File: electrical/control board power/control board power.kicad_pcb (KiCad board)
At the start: 2 copper layers, 147.3 x 147.3 mm, 67 parts, among them J1 Conn_01x02, J10 48V_from_conversion, J11 Aux_2, J17 Switch_B, J2 5V, J3 Barrel_Jack, J4 Switch_A, J5 Switch_Input, J6 Power_Connector, J7 Switch_A_High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

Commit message: stuff
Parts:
- moved Q2 6.48 mm to (132.0, 63.1)
- moved J17 5.21 mm to (141.4, 82.4)
- moved C24 5.08 mm to (139.6, 91.9)
- moved J8 5.08 mm to (134.5, 87.6)
- moved D10 3.86 mm to (133.0, 79.5)
- moved J4 2.03 mm to (124.2, 82.4)
- moved D9 1.17 mm to (116.1, 79.6)
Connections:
- C23 pad 1: Net-(C23-Pad1) -> GND
- C24 pad 1: Net-(C23-Pad1) -> GND
- Q1 pad 3: Net-(C23-Pad1) -> GND
- Q2 pad 3: Net-(C23-Pad1) -> GND
- R4 pad 2: Net-(C23-Pad1) -> GND
- R5 pad 2: Net-(C23-Pad1) -> GND
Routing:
- net GND: track 111.8 -> 122.8 mm, vias 69 -> 75
- net +24V: track 227.7 -> 218.9 mm
- net Net-(C23-Pad1): track 8.21 -> 0.00 mm, vias 6 -> 0
- net /SWITCH_B: track 16.4 -> 23.4 mm
- net +5V: track 289.4 -> 284.4 mm
- net Net-(C7-Pad1): track 14.7 -> 11.6 mm
- net Net-(C8-Pad2): track 12.4 -> 9.75 mm
- net /SWITCH_B_HIGH: track 18.3 -> 21.0 mm
- net /SWITCH_A_HIGH: track 19.6 -> 21.4 mm
- net Net-(D9-Pad2): track 18.8 -> 19.3 mm

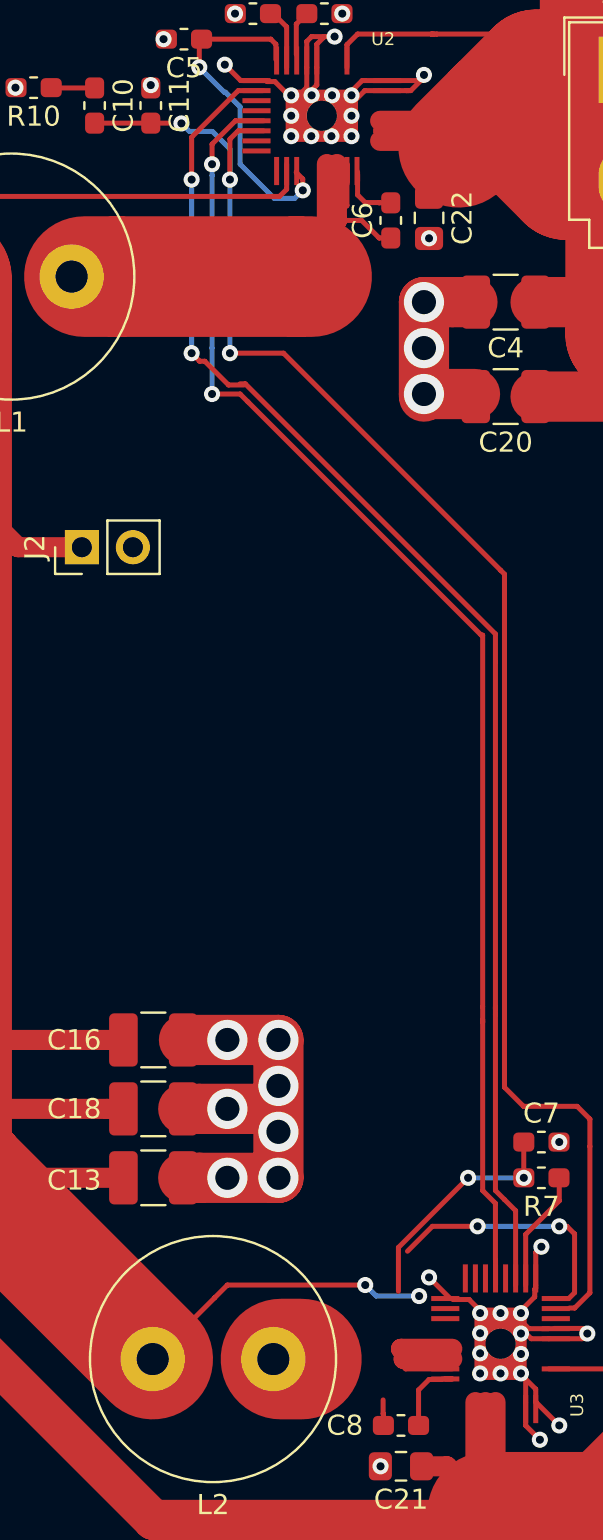
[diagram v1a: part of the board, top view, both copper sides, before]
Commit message: fixed unconnected parts
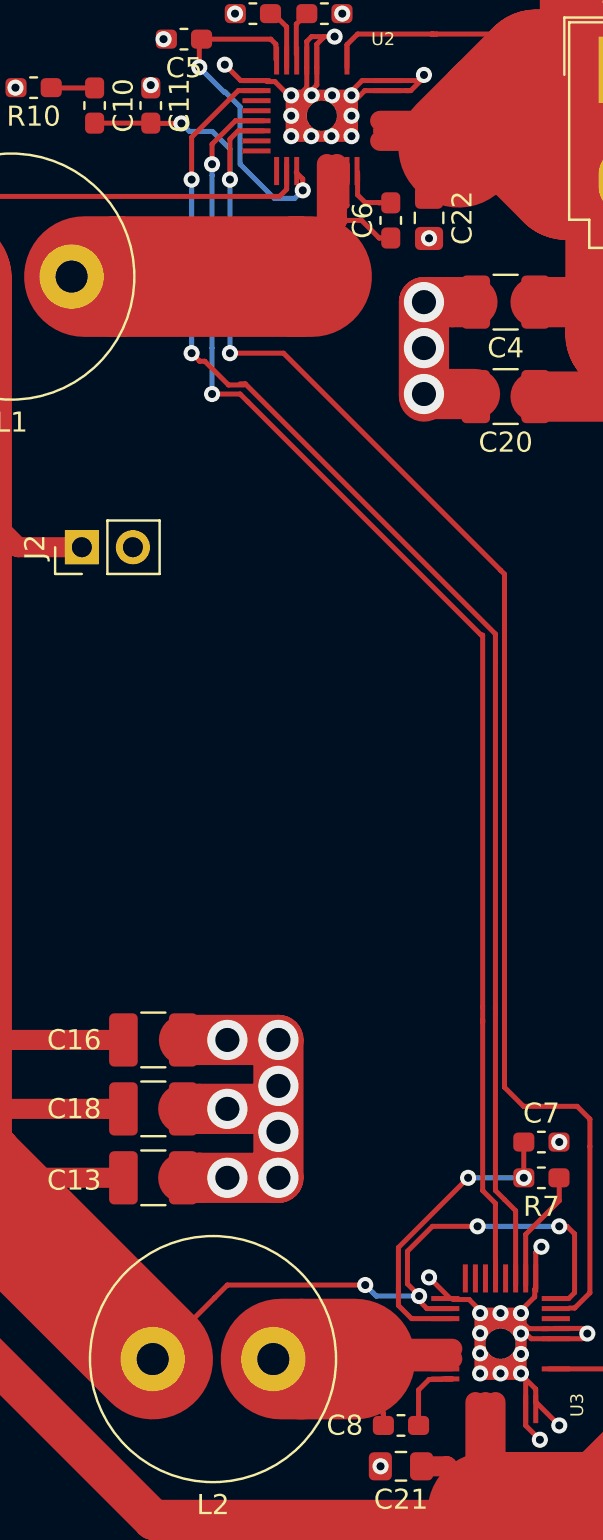
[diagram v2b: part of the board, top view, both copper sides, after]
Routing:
- net Net-(C8-Pad2): track 9.75 -> 14.6 mm
- net +5V: track 284.4 -> 289.0 mm
- net Net-(C7-Pad1): track 11.6 -> 15.5 mm
- net Net-(C10-Pad2): track 79.2 -> 79.8 mm
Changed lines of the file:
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@@
     (thickness 1.6)
     (drawings 27)
-    (tracks 576)
+    (tracks 586)
     (zones 0)
     (modules 67)
@@
   (segment (start 49.149 150.622) (end 49.149 126.238) (width 0.25) (layer F.Cu) (net 8))
   (segment (start 49.149 126.238) (end 49.149 126.111) (width 0.25) (layer F.Cu) (net 8))
+  (segment (start 96.161998 119.916) (end 95.758 119.512002) (width 0.25) (layer F.Cu) (net 8))
+  (segment (start 97.422 119.916) (end 96.161998 119.916) (width 0.25) (layer F.Cu) (net 8))
+  (segment (start 95.758 119.512002) (end 95.758 119.253) (width 0.25) (layer F.Cu) (net 8))
+  (segment (start 95.19201 117.0634) (end 95.19201 118.68701) (width 0.25) (layer F.Cu) (net 8))
+  (segment (start 95.19201 118.68701) (end 95.758 119.253) (width 0.25) (layer F.Cu) (net 8))
   (via (at 61.976 116.205) (size 2) (drill 1.2) (layers F.Cu B.Cu) (net 9))
   (segment (start 51.199 121.627) (end 56.621 116.205) (width 2) (layer F.Cu) (net 9) (status 10))
@@
   (segment (start 98.208 113.411) (end 94.742 116.877) (width 0.25) (layer F.Cu) (net 13))
   (segment (start 94.742 116.877) (end 94.742 119.056002) (width 0.25) (layer F.Cu) (net 13))
+  (segment (start 97.422 120.416) (end 95.397 120.416) (width 0.25) (layer F.Cu) (net 13))
+  (segment (start 95.397 120.416) (end 94.742 119.761) (width 0.25) (layer F.Cu) (net 13))
+  (segment (start 94.742 119.761) (end 94.742 118.872) (width 0.25) (layer F.Cu) (net 13))
   (segment (start 94.873 121.916) (end 94.869 121.92) (width 1) (layer F.Cu) (net 14))
   (segment (start 97.422 121.916) (end 94.873 121.916) (width 1) (layer F.Cu) (net 14) (status 10))
@@
   (segment (start 93.994 125.73) (end 93.994 125.155) (width 0.25) (layer F.Cu) (net 14) (status 10))
   (segment (start 93.98 125.141) (end 93.98 124.46) (width 0.25) (layer F.Cu) (net 14))
+  (segment (start 93.98 124.46) (end 92.456 122.936) (width 0.25) (layer F.Cu) (net 14))
+  (segment (start 89.916 122.428) (end 92.579726 122.428) (width 6) (layer F.Cu) (net 14))
   (segment (start 97.422 123.416) (end 96.929 123.416) (width 0.25) (layer F.Cu) (net 15) (status 30))
   (segment (start 97.422 123.416) (end 97.056 123.416) (width 0.25) (layer F.Cu) (net 15) (status 30))
@@
   (segment (start 79.629 59.196) (end 77.611 59.196) (width 0.25) (layer F.Cu) (net 17) (status 30))
   (segment (start 77.611 59.196) (end 77.597 59.182) (width 0.25) (layer F.Cu) (net 17) (status 30))
-  (segment (start 82.423 60.946) (end 83.298 60.946) (width 0.25) (layer F.Cu) (net 18) (status 10))
   (segment (start 82.423 60.946) (end 79.742 60.946) (width 0.25) (layer F.Cu) (net 18) (status 30))
   (segment (start 79.742 60.946) (end 79.629 60.833) (width 0.25) (layer F.Cu) (net 18) (status 30))
@@
   (segment (start 85.489999 61.359999) (end 86.36 62.23) (width 0.25) (layer B.Cu) (net 18))
   (segment (start 86.36 62.23) (end 86.36 63.627) (width 0.25) (layer B.Cu) (net 18))
+  (segment (start 83.947 60.96) (end 82.423 60.96) (width 0.25) (layer F.Cu) (net 18))
   (segment (start 102.743 114.554) (end 102.743 113.411) (width 0.25) (layer F.Cu) (net 19) (status 20))
   (segment (start 101.072 116.225) (end 102.743 114.554) (width 0.25) (layer F.Cu) (net 19))

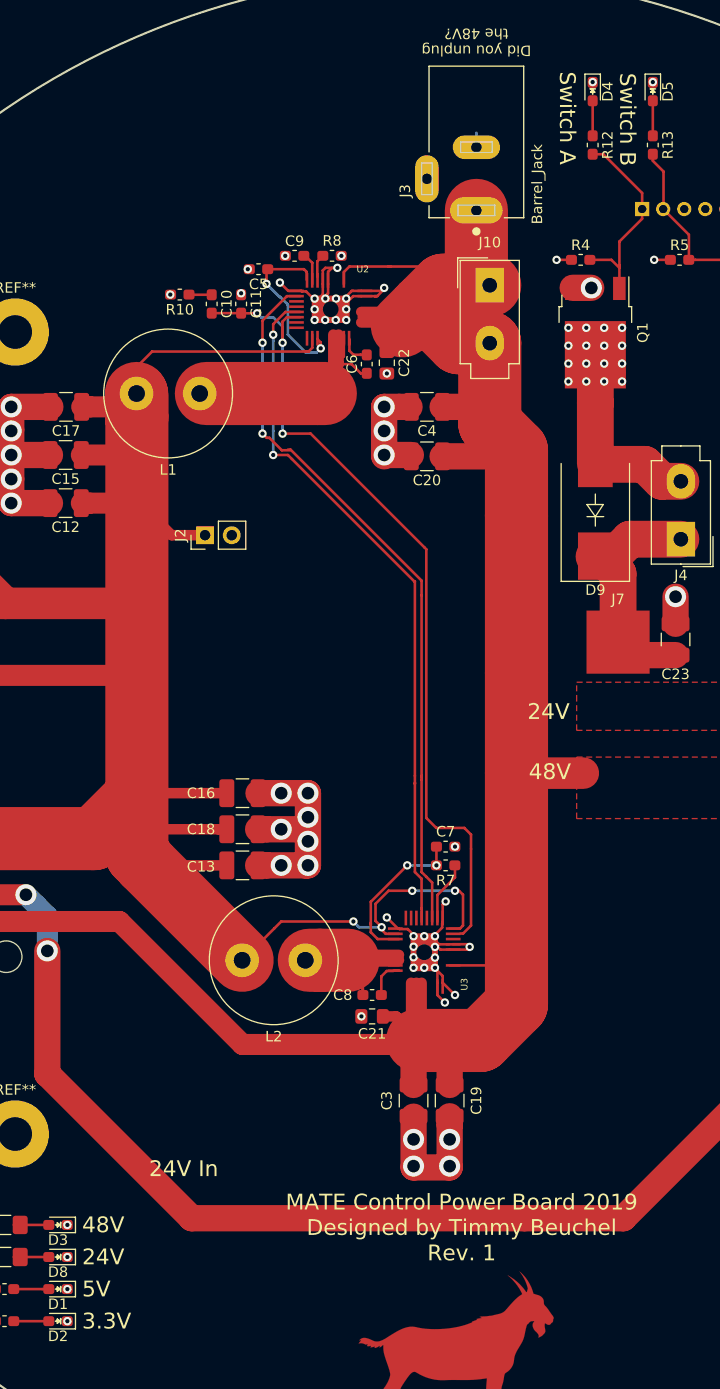
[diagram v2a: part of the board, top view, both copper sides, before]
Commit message: Removed most of the via in pads
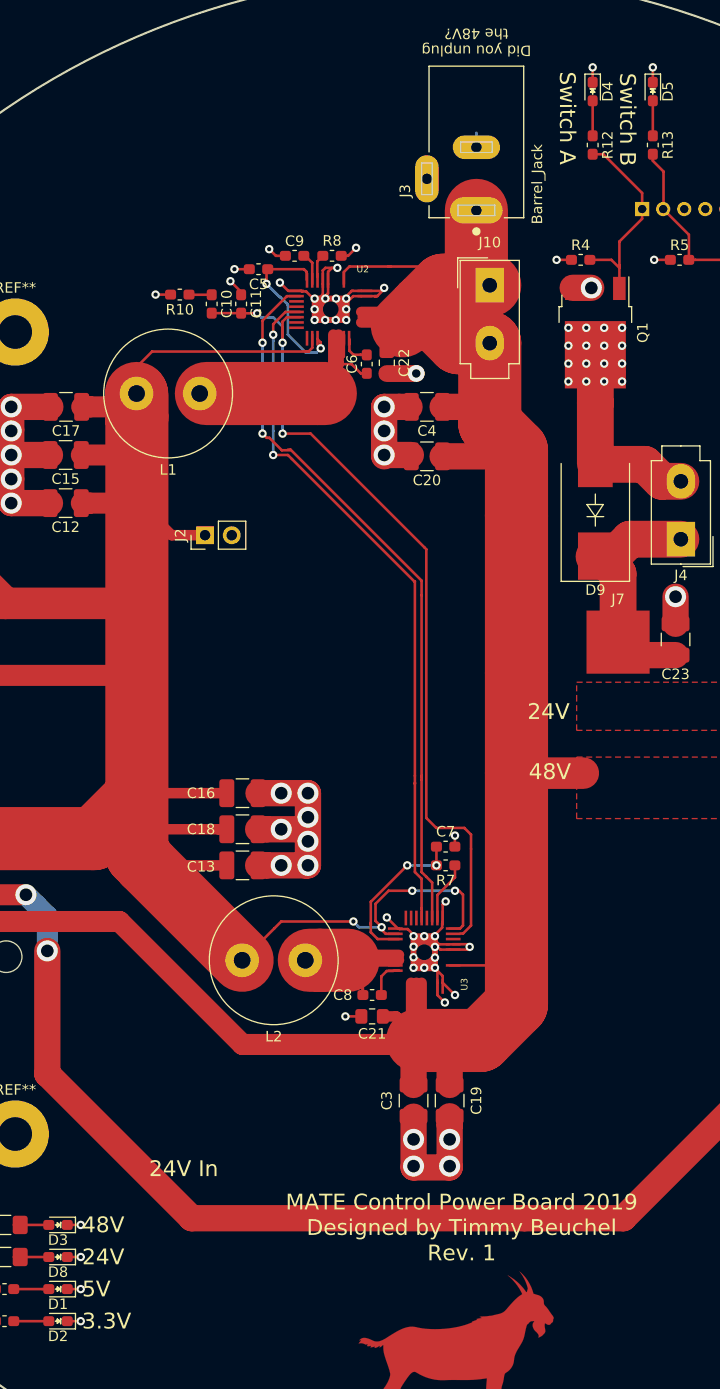
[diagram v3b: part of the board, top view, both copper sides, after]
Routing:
- net GND: track 122.8 -> 144.2 mm
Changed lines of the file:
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@@
     (thickness 1.6)
     (drawings 27)
-    (tracks 586)
+    (tracks 605)
     (zones 0)
     (modules 67)
@@
   )
   (gr_circle (center 101.6 102.362) (end 175.26 102.362) (layer Edge.Cuts) (width 0.2))
-  (via (at 91.948 55.499) (size 0.8) (drill 0.4) (layers F.Cu B.Cu) (net 1) (status 30))
-  (via (at 86.614 55.499) (size 0.8) (drill 0.4) (layers F.Cu B.Cu) (net 1) (status 30))
-  (via (at 75.692 59.182) (size 0.8) (drill 0.4) (layers F.Cu B.Cu) (net 1) (status 30))
   (via (at 102.235 141.986) (size 2) (drill 1.2) (layers F.Cu B.Cu) (net 1))
   (via (at 98.806 141.986) (size 2) (drill 1.2) (layers F.Cu B.Cu) (net 1))
@@
   (via (at 88.773 113.411) (size 2) (drill 1.2) (layers F.Cu B.Cu) (net 1))
   (via (at 86.233 113.411) (size 2) (drill 1.2) (layers F.Cu B.Cu) (net 1))
-  (via (at 93.853 127.762) (size 0.8) (drill 0.4) (layers F.Cu B.Cu) (net 1) (status 30))
-  (via (at 102.743 111.633) (size 0.8) (drill 0.4) (layers F.Cu B.Cu) (net 1) (status 30))
-  (via (at 96.266 66.675) (size 0.8) (drill 0.4) (layers F.Cu B.Cu) (net 1) (status 30))
-  (via (at 65.913 150.622) (size 0.8) (drill 0.4) (layers F.Cu B.Cu) (net 1) (status 30))
-  (via (at 65.913 147.574) (size 0.8) (drill 0.4) (layers F.Cu B.Cu) (net 1) (status 30))
-  (via (at 65.913 153.67) (size 0.8) (drill 0.4) (layers F.Cu B.Cu) (net 1) (status 30))
-  (via (at 65.913 156.718) (size 0.8) (drill 0.4) (layers F.Cu B.Cu) (net 1) (status 30))
   (via (at 100.838 123.142) (size 0.8) (drill 0.4) (layers F.Cu B.Cu) (net 1) (status 30))
   (via (at 100.838 120.142) (size 0.8) (drill 0.4) (layers F.Cu B.Cu) (net 1) (status 30))
@@
   (via (at 98.806 120.142) (size 0.8) (drill 0.4) (layers F.Cu B.Cu) (net 1) (status 30))
   (via (at 89.408 61.595) (size 0.8) (drill 0.4) (layers F.Cu B.Cu) (net 1) (status 30))
-  (via (at 115.824 38.989) (size 0.8) (drill 0.4) (layers F.Cu B.Cu) (net 1) (status 30))
-  (via (at 121.539 38.989) (size 0.8) (drill 0.4) (layers F.Cu B.Cu) (net 1) (status 30))
-  (via (at 82.423 59.055) (size 0.8) (drill 0.4) (layers F.Cu B.Cu) (net 1) (status 30))
-  (via (at 83.058 56.769) (size 0.8) (drill 0.4) (layers F.Cu B.Cu) (net 1) (status 30))
   (via (at 53.075 99.557) (size 0.8) (drill 0.4) (layers F.Cu B.Cu) (net 1) (status 30))
   (via (at 53.975 100.457) (size 0.8) (drill 0.4) (layers F.Cu B.Cu) (net 1) (status 30))
@@
   (via (at 112.395 55.88) (size 0.8) (drill 0.4) (layers F.Cu B.Cu) (net 1))
   (segment (start 113.806 55.88) (end 112.395 55.88) (width 0.25) (layer F.Cu) (net 1))
+  (via (at 102.743 110.58) (size 0.8) (drill 0.4) (layers F.Cu B.Cu) (net 1))
+  (segment (start 102.729 111.633) (end 102.729 110.594) (width 0.25) (layer F.Cu) (net 1))
+  (segment (start 102.729 110.594) (end 102.743 110.58) (width 0.25) (layer F.Cu) (net 1))
+  (via (at 92.329 127.762) (size 0.8) (drill 0.4) (layers F.Cu B.Cu) (net 1))
+  (segment (start 93.844 127.762) (end 92.329 127.762) (width 0.25) (layer F.Cu) (net 1))
+  (via (at 67.183 147.574) (size 0.8) (drill 0.4) (layers F.Cu B.Cu) (net 1))
+  (segment (start 65.899 147.574) (end 67.183 147.574) (width 0.25) (layer F.Cu) (net 1))
+  (via (at 67.183 150.622) (size 0.8) (drill 0.4) (layers F.Cu B.Cu) (net 1))
+  (segment (start 65.899 150.622) (end 67.183 150.622) (width 0.25) (layer F.Cu) (net 1))
+  (via (at 67.183 153.67) (size 0.8) (drill 0.4) (layers F.Cu B.Cu) (net 1))
+  (segment (start 65.899 153.67) (end 67.183 153.67) (width 0.25) (layer F.Cu) (net 1))
+  (via (at 67.183 156.718) (size 0.8) (drill 0.4) (layers F.Cu B.Cu) (net 1))
+  (segment (start 65.899 156.718) (end 67.183 156.718) (width 0.25) (layer F.Cu) (net 1))
+  (via (at 74.295 59.182) (size 0.8) (drill 0.4) (layers F.Cu B.Cu) (net 1))
+  (segment (start 75.72 59.182) (end 74.295 59.182) (width 0.25) (layer F.Cu) (net 1))
+  (via (at 81.407 57.912) (size 0.8) (drill 0.4) (layers F.Cu B.Cu) (net 1))
+  (segment (start 82.423 59.196) (end 82.423 58.928) (width 0.25) (layer F.Cu) (net 1))
+  (segment (start 82.423 58.928) (end 81.407 57.912) (width 0.25) (layer F.Cu) (net 1))
+  (via (at 81.788 56.769) (size 0.8) (drill 0.4) (layers F.Cu B.Cu) (net 1))
+  (segment (start 83.199 56.769) (end 81.788 56.769) (width 0.25) (layer F.Cu) (net 1))
+  (via (at 85.09 54.864) (size 0.8) (drill 0.4) (layers F.Cu B.Cu) (net 1))
+  (segment (start 86.628 55.499) (end 85.725 55.499) (width 0.25) (layer F.Cu) (net 1))
+  (segment (start 85.725 55.499) (end 85.09 54.864) (width 0.25) (layer F.Cu) (net 1))
+  (via (at 93.345 54.737) (size 0.8) (drill 0.4) (layers F.Cu B.Cu) (net 1))
+  (segment (start 91.934 55.499) (end 92.583 55.499) (width 0.25) (layer F.Cu) (net 1))
+  (segment (start 92.583 55.499) (end 93.345 54.737) (width 0.25) (layer F.Cu) (net 1))
+  (via (at 99.06 66.675) (size 1.6) (drill 0.8) (layers F.Cu B.Cu) (net 1))
+  (segment (start 96.266 66.684) (end 99.051 66.684) (width 1.6) (layer F.Cu) (net 1))
+  (segment (start 99.051 66.684) (end 99.06 66.675) (width 1.6) (layer F.Cu) (net 1))
+  (via (at 115.824 37.592) (size 0.8) (drill 0.4) (layers F.Cu B.Cu) (net 1))
+  (segment (start 115.824 39.017) (end 115.824 37.592) (width 0.25) (layer F.Cu) (net 1))
+  (via (at 121.539 37.592) (size 0.8) (drill 0.4) (layers F.Cu B.Cu) (net 1))
+  (segment (start 121.539 39.017) (end 121.539 37.592) (width 0.25) (layer F.Cu) (net 1))
   (via (at 53.848 98.171) (size 0.8) (drill 0.4) (layers F.Cu B.Cu) (net 2) (status 30))
   (via (at 47.73 99.016) (size 0.8) (drill 0.4) (layers F.Cu B.Cu) (net 2) (status 30))
